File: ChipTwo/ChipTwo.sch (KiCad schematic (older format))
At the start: 27 parts, among them J1 Conn_Coaxial, J2 Conn_Coaxial, J3 5767007-8, J4 5767007-8, U1 Y1247AstimulusGenerator, U11 3pinSwitchCustom, U2 Y1247AstimulusGenerator, U3 Y1247AstimulusGenerator, U4 Y1247AstimulusGenerator, U5 CHIP2, U6 3pinSwitchCustom

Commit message: Switch changed in both the layout
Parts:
- U11, U6: footprint Pin_Headers:Pin_Header_Straight_1x03_Pitch2.54mm -> SW_MS12ANW03:SW_MS12ANW03
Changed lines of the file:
@@
 F 0 "U6" H 2150 1692 50  0000 C CNN
 F 1 "3pinSwitchCustom" H 2150 1601 50  0000 C CNN
-F 2 "Pin_Headers:Pin_Header_Straight_1x03_Pitch2.54mm" H 2200 1100 50  0001 C CNN
+F 2 "SW_MS12ANW03:SW_MS12ANW03" H 2200 1100 50  0001 C CNN
 F 3 "http://www.ti.com/lit/ds/symlink/ts5a3159.pdf" H 2150 1450 50  0001 C CNN
 	1    2150 1450
@@
 F 0 "U11" H 2150 2642 50  0000 C CNN
 F 1 "3pinSwitchCustom" H 2150 2551 50  0000 C CNN
-F 2 "Pin_Headers:Pin_Header_Straight_1x03_Pitch2.54mm" H 2200 2050 50  0001 C CNN
+F 2 "SW_MS12ANW03:SW_MS12ANW03" H 2200 2050 50  0001 C CNN
 F 3 "http://www.ti.com/lit/ds/symlink/ts5a3159.pdf" H 2150 2400 50  0001 C CNN
 	1    2150 2400

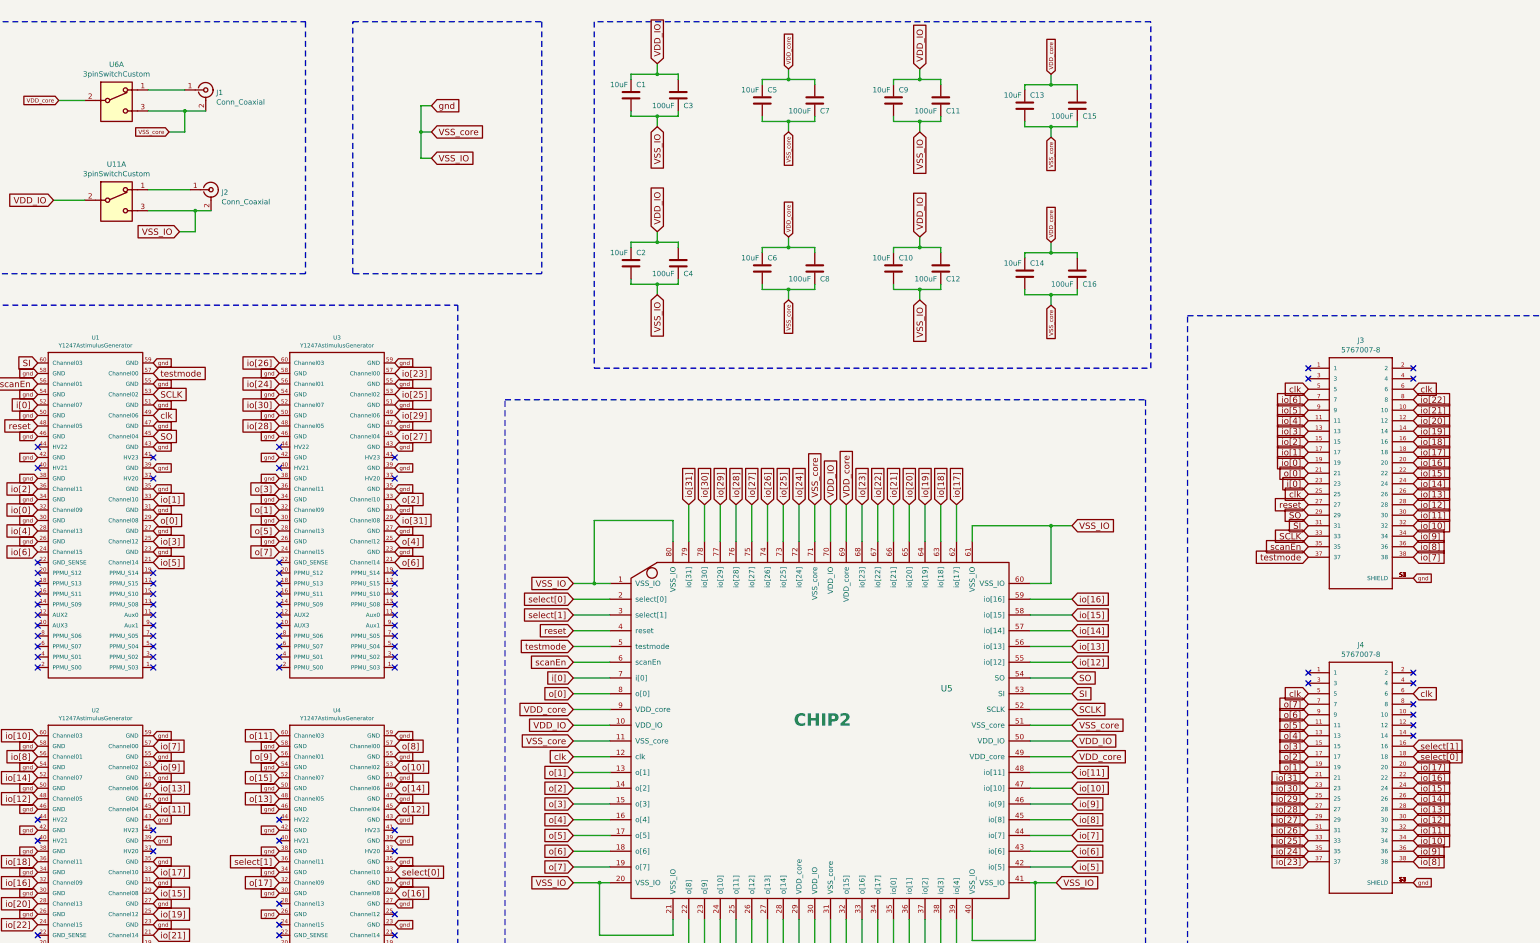
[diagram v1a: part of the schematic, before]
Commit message: Checking for chip two completed, Combined PCB updated
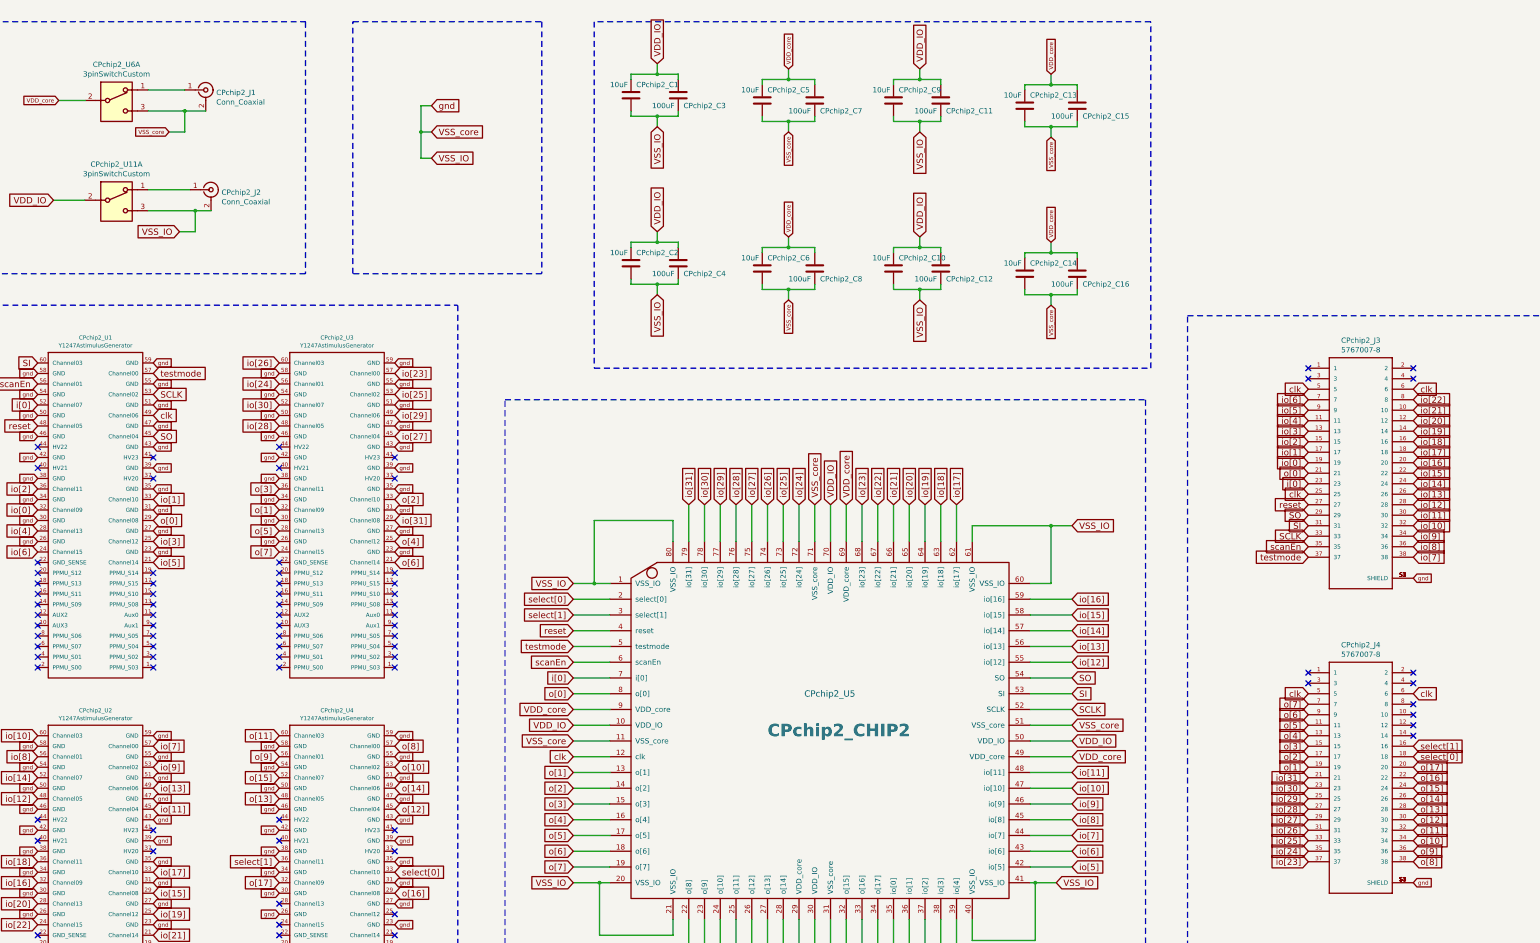
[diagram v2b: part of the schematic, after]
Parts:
- CPchip2_U5: renamed from U5; value CHIP2 -> CPchip2_CHIP2
- renumbered C1 to CPchip2_C1, C10 to CPchip2_C10, C11 to CPchip2_C11, C12 to CPchip2_C12, C13 to CPchip2_C13, C14 to CPchip2_C14, C15 to CPchip2_C15, C16 to CPchip2_C16, C2 to CPchip2_C2, C3 to CPchip2_C3, C4 to CPchip2_C4, C5 to CPchip2_C5, C6 to CPchip2_C6, C7 to CPchip2_C7, C8 to CPchip2_C8, C9 to CPchip2_C9, J1 to CPchip2_J1, J2 to CPchip2_J2, J3 to CPchip2_J3, J4 to CPchip2_J4, U1 to CPchip2_U1, U11 to CPchip2_U11, U2 to CPchip2_U2, U3 to CPchip2_U3, U4 to CPchip2_U4, U6 to CPchip2_U6
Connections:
- net io[10]: no longer CPchip2_J4.34
- net io[11]: no longer CPchip2_J4.32
- net io[12]: no longer CPchip2_J4.30
- net io[13]: no longer CPchip2_J4.28
- net io[14]: no longer CPchip2_J4.26
- net io[15]: no longer CPchip2_J4.24
- net io[16]: no longer CPchip2_J4.22
- net io[17]: no longer CPchip2_J4.20
- net io[8]: no longer CPchip2_J4.38
- net io[9]: no longer CPchip2_J4.36
- net o[10]: now also CPchip2_J4.34
- net o[11]: now also CPchip2_J4.32
- net o[12]: now also CPchip2_J4.30
- net o[13]: now also CPchip2_J4.28
- net o[14]: now also CPchip2_J4.26
- net o[15]: now also CPchip2_J4.24
- net o[16]: now also CPchip2_J4.22
- net o[17]: now also CPchip2_J4.20
- net o[8]: now also CPchip2_J4.38
- net o[9]: now also CPchip2_J4.36
